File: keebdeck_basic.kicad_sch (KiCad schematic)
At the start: 108 parts, among them J1 USB_C_Receptacle_USB2.0, J2 Conn_Qwiic, SW1 SW_ESC, SW10 SW_1, SW11 SW_2, SW12 SW_3, SW13 SW_4, SW14 SW_5, SW15 SW_6, SW16 SW_7, SW17 SW_8, SW18 SW_9, SW19 SW_0, SW2 SW_SQUARE, SW20 SW_-, SW21 SW_=, SW22 SW_TAB, SW23 SW_Q, SW24 SW_W, SW25 SW_E, SW26 SW_R, SW27 SW_T, SW28 SW_Y, SW29 SW_U, SW3 SW_TRIANGLE, SW30 SW_I, SW31 SW_O, SW32 SW_P, SW33 SW_[, SW34 SW_], SW35 SW_FN, SW36 SW_A, SW37 SW_S, SW38 SW_D, SW39 SW_F, SW4 SW_CROSS, SW40 SW_G, SW41 SW_H, SW42 SW_J, SW43 SW_K, SW44 SW_L, SW45 SW_;, SW46 SW_', SW47 SW_ENTER, SW48 SW_LSHIFT, SW49 SW_Z, SW5 SW_CIRCLE, SW50 SW_X, SW51 SW_C, SW52 SW_V, SW53 SW_B, SW54 SW_N, SW55 SW_M, SW56 SW_,, SW57 SW_., SW58 SW_/, SW59 SW_UP, SW6 SW_CLUB, SW60 SW_RSHIFT, SW61 SW_CTRL, SW62 SW_SP, SW63 SW_LALT, SW64 SW_\, SW65 SW_SPACE1, SW66 SW_SPACE2, SW67 SW_SPACE3, SW68 SW_RALT, SW69 SW_LEFT, SW7 SW_DIAMOND, SW70 SW_DOWN, SW71 SW_RIGHT, SW72 SW_BOOT, SW8 SW_BACKSPACE, SW9 SW_TILDE, U1 AP3032KTR, U2 AP2112K-3.3, U3 STM32F042G6Ux

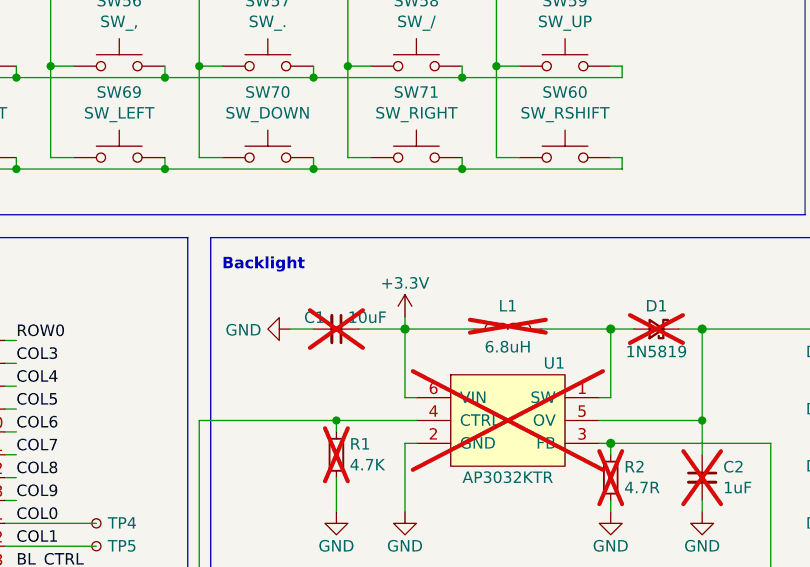
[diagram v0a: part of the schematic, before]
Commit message: Efficiency and EMI improvements
Changed the voltage supply for the backlight from +3.3V to +5V. This should improve the power efficiency slightly, as the AP3032 is more efficient at 5V input, and the LDO needs to handle less current.

Also added vias next to the GND pads of the USB-C connector, this might slightly improve EMI at no extra costs.
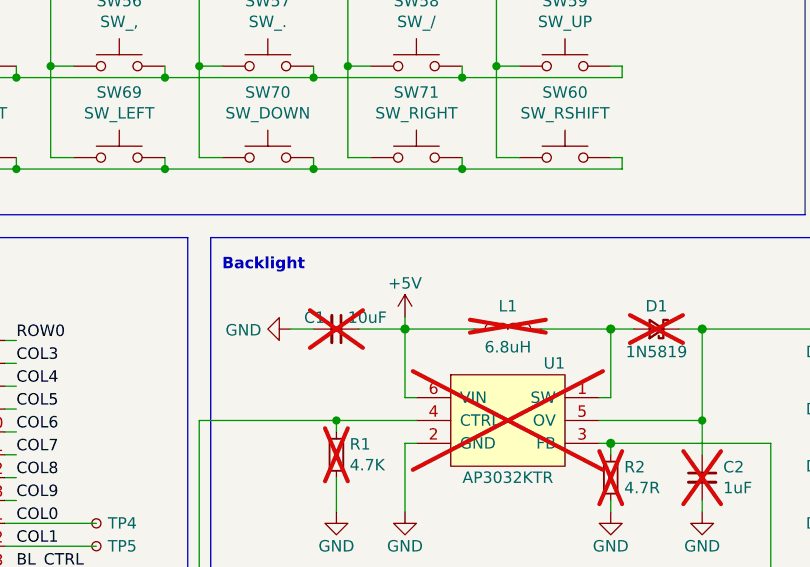
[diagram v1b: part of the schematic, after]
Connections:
- net +3.3V: no longer C1.1, L1.1, U1.6 (VIN)
- net +5V: now also C1.1, L1.1, U1.6 (VIN)
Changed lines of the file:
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@@
-	)
-	(symbol
-		(lib_name "+3.3V_2")
-		(lib_id "power:+3.3V")
-		(at 220.98 111.76 0)
-		(unit 1)
-		(exclude_from_sim no)
-		(in_bom yes)
-		(on_board yes)
-		(dnp no)
-		(fields_autoplaced yes)
-		(property "Reference" "#PWR08"
-			(at 220.98 115.57 0)
-			(effects
-				(font
-					(size 1.27 1.27)
-				)
-				(hide yes)
-			)
-		)
-		(property "Value" "+3.3V"
-			(at 220.98 107.95 0)
-			(effects
-				(font
-					(size 1.27 1.27)
-				)
-			)
-		)
-		(property "Footprint" ""
-			(at 220.98 111.76 0)
-			(effects
-				(font
-					(size 1.27 1.27)
-				)
-			)
-		)
-		(property "Datasheet" ""
-			(at 220.98 111.76 0)
-			(effects
-				(font
-					(size 1.27 1.27)
-				)
-			)
-		)
-		(property "Description" ""
-			(at 220.98 111.76 0)
-			(effects
-				(font
-					(size 1.27 1.27)
-				)
-			)
-		)
-		(pin "1"
-		)
-		(instances
-			(project "keebdeck_basic"
-				(path "/aa8956e0-d53c-4a9f-8300-ac6f31c01c20"
-					(reference "#PWR08")
-					(unit 1)
-				)
-			)
-		)
 	)
 	(symbol
@@
 					(unit 1)
 				)
+			)
+		)
+	)
+	(symbol
+		(lib_id "power:+5V")
+		(at 220.98 111.76 0)
+		(unit 1)
+		(exclude_from_sim no)
+		(in_bom yes)
+		(on_board yes)
+		(dnp no)
+		(property "Reference" "#PWR08"
+			(at 220.98 115.57 0)
+			(effects
+				(font
+					(size 1.27 1.27)
+				)
+				(hide yes)
+			)
+		)
+		(property "Value" "+5V"
+			(at 220.98 107.95 0)
+			(effects
+				(font
+					(size 1.27 1.27)
+				)
+			)
+		)
+		(property "Footprint" ""
+			(at 220.98 111.76 0)
+			(effects
+				(font
+					(size 1.27 1.27)
+				)
+				(hide yes)
+			)
+		)
+		(property "Datasheet" ""
+			(at 220.98 111.76 0)
+			(effects
+				(font
+					(size 1.27 1.27)
+				)
+				(hide yes)
+			)
+		)
+		(property "Description" "Power symbol creates a global label with name \"+5V\""
+			(at 220.98 111.76 0)
+			(effects
+				(font
+					(size 1.27 1.27)
+				)
+				(hide yes)
+			)
+		)
+		(pin "1"
+		)
+		(instances
+			(project "keebdeck_basic"
+				(path "/aa8956e0-d53c-4a9f-8300-ac6f31c01c20"
+					(reference "#PWR08")
+					(unit 1)
+				)
